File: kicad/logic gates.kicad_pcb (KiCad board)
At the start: 2 copper layers, 33 parts, among them J1 USB_B_Micro, Q1 NPN, Q2 NPN, Q3 NPN, Q4 NPN, Q5 NPN, Q6 NPN, Q7 NPN, SW1 SW_SPST, SW2 SW_SPST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

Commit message: pcb cleanup
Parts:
- moved J1 24.0 mm to (91.2, 16.4)
- moved SW6 23.0 mm to (82.0, 16.0)
- moved R11 2.01 mm to (134.5, 46.1), turned to 90 degrees
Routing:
- net Net-(D4-K): track 595.8 -> 547.7 mm
- net Net-(Q7-B): track 51.3 -> 64.4 mm
- net Net-(Q6-C): track 24.8 -> 26.4 mm
- net Net-(D3-K): track 291.1 -> 292.5 mm
- net Net-(J1-VBUS): track 9.02 -> 9.92 mm
- net Net-(D1-K): track 51.5 -> 50.8 mm

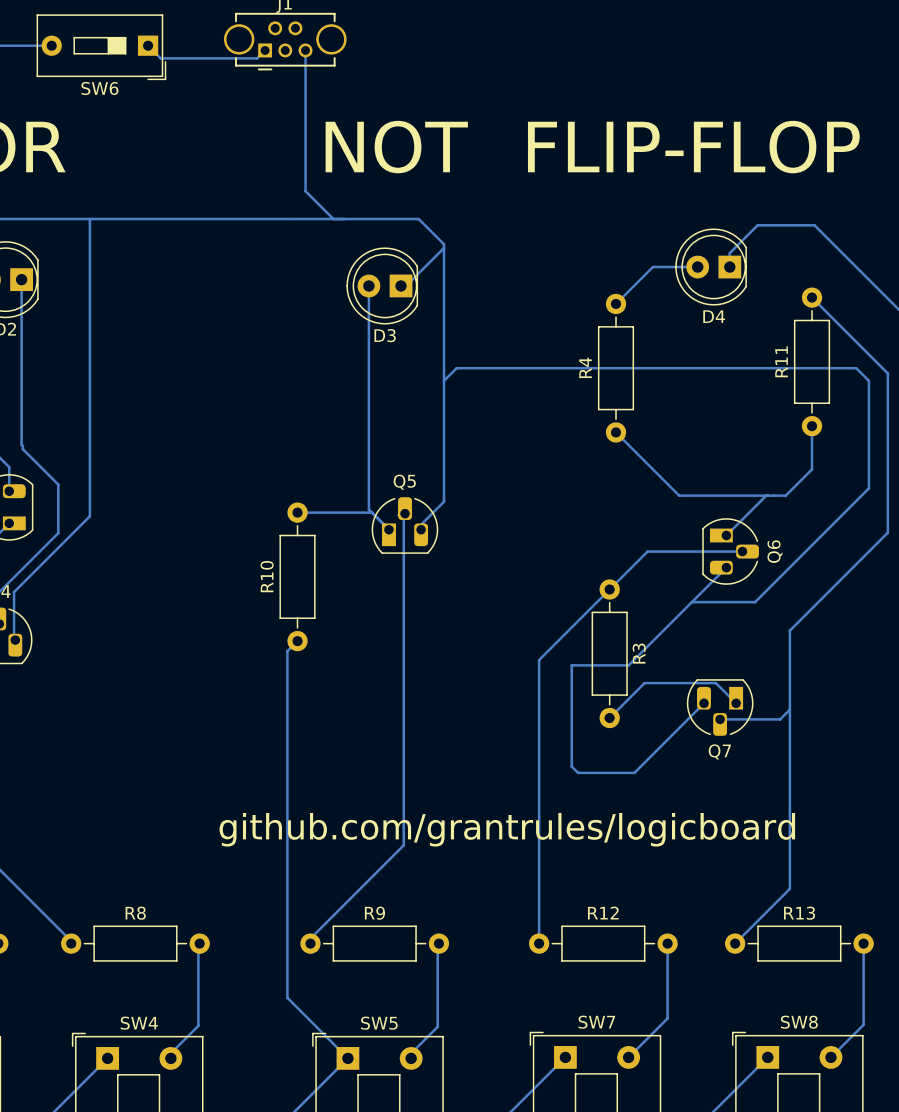
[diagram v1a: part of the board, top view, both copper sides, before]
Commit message: fixed names and values
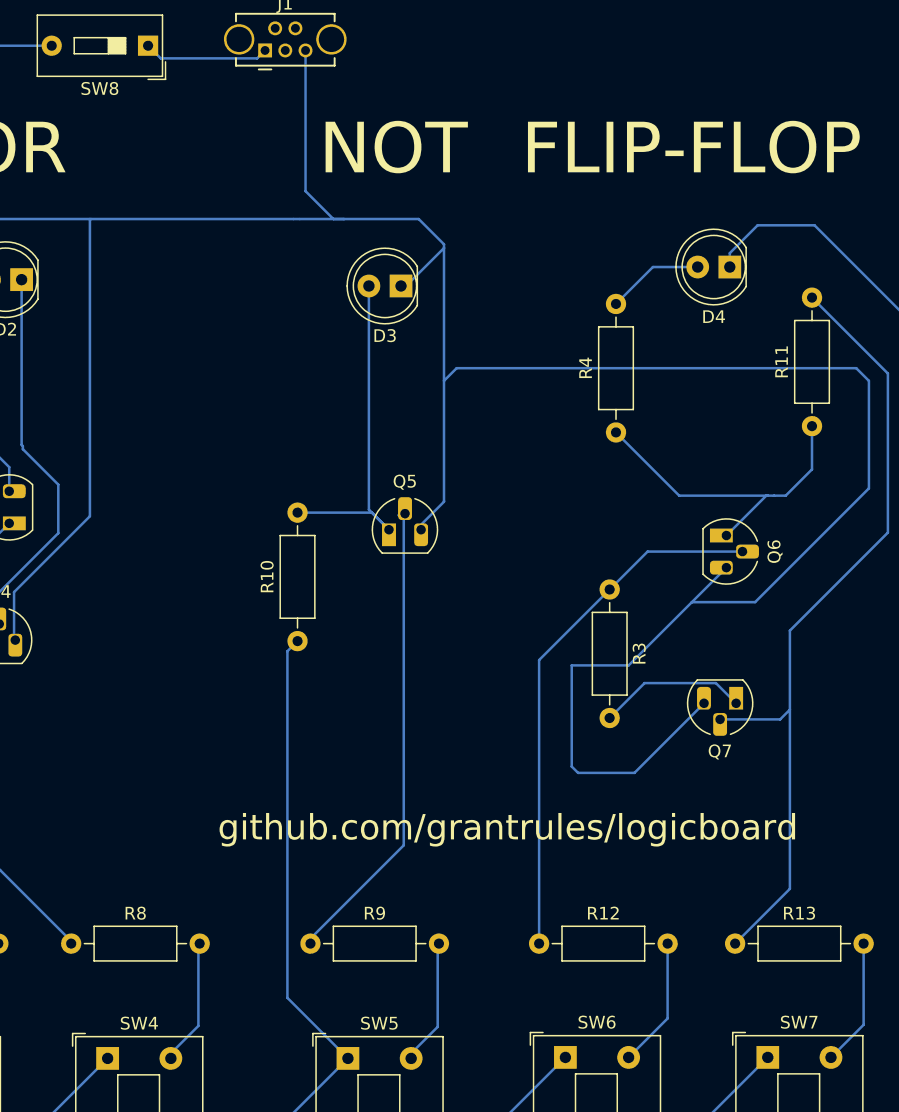
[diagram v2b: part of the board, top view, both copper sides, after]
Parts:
- R10: value 350 -> 345
- R2, R4: value R345 -> 345
- renumbered SW7 to SW6, SW8 to SW7, SW6 to SW8
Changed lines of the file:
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@@
 	(net 28 "Net-(Q7-C)")
 	(net 29 "Net-(SW7-B)")
-	(net 30 "Net-(SW8-B)")
+	(net 30 "Net-(SW6-B)")
 	(footprint "LED_THT:LED_D5.0mm"
 		(layer "F.Cu")
@@
 			)
 		)
-		(property "Value" "R345"
+		(property "Value" "345"
 			(at 5.08 2.37 90)
 			(layer "F.Fab")
@@
 			)
 		)
-		(property "Value" "350"
+		(property "Value" "345"
 			(at 5.08 2.37 90)
 			(layer "F.Fab")
@@
 			(layers "*.Cu" "*.Mask")
 			(remove_unused_layers no)
-			(net 29 "Net-(SW7-B)")
+			(net 30 "Net-(SW6-B)")
 			(pintype "passive")
 		)
@@
 		(descr "momentary / push-push button, h=17.5mm C&K PVA1 https://www.ckswitches.com/media/1343/pva.pdf")
 		(tags "tact sw push PVA1 DPST")
-		(property "Reference" "SW7"
+		(property "Reference" "SW6"
 			(at 2.5 -2.75 0)
 			(layer "F.SilkS")
@@
 			(layers "*.Cu" "*.Mask")
 			(remove_unused_layers no)
-			(net 29 "Net-(SW7-B)")
+			(net 30 "Net-(SW6-B)")
 			(pinfunction "B")
 			(pintype "passive")
@@
 			(layers "*.Cu" "*.Mask")
 			(remove_unused_layers no)
-			(net 30 "Net-(SW8-B)")
+			(net 29 "Net-(SW7-B)")
 			(pintype "passive")
 		)
@@
 		(descr "1x-dip-switch SPST , Slide, row spacing 7.62 mm (300 mils), body size 9.78x4.72mm (see e.g. https://www.ctscorp.com/wp-content/uploads/206-208.pdf)")
 		(tags "DIP Switch SPST Slide 7.62mm 300mil")
-		(property "Reference" "SW6"
+		(property "Reference" "SW8"
 			(at 3.81 -3.42 0)
 			(layer "F.SilkS")
@@
 		(descr "momentary / push-push button, h=17.5mm C&K PVA1 https://www.ckswitches.com/media/1343/pva.pdf")
 		(tags "tact sw push PVA1 DPST")
-		(property "Reference" "SW8"
+		(property "Reference" "SW7"
 			(at 2.5 -2.75 0)
 			(layer "F.SilkS")
@@
 			(layers "*.Cu" "*.Mask")
 			(remove_unused_layers no)
-			(net 30 "Net-(SW8-B)")
+			(net 29 "Net-(SW7-B)")
 			(pinfunction "B")
 			(pintype "passive")
@@
 			)
 		)
-		(property "Value" "R345"
+		(property "Value" "345"
 			(at 5.08 2.37 90)
 			(layer "F.Fab")
@@
 	)
 	(segment
-		(start 123.08 92.92)
-		(end 123.08 87)
+		(start 138.58 93.42)
+		(end 138.58 87)
 		(width 0.2)
 		(layer "B.Cu")
@@
 	)
 	(segment
-		(start 120 96)
-		(end 123.08 92.92)
+		(start 136 96)
+		(end 138.58 93.42)
 		(width 0.2)
 		(layer "B.Cu")
@@
 	)
 	(segment
-		(start 138.58 93.42)
-		(end 138.58 87)
+		(start 123.08 92.92)
+		(end 123.08 87)
 		(width 0.2)
 		(layer "B.Cu")
@@
 	)
 	(segment
-		(start 136 96)
-		(end 138.58 93.42)
+		(start 120 96)
+		(end 123.08 92.92)
 		(width 0.2)
 		(layer "B.Cu")

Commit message: fix pcb
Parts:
- J1: value USB_B_Micro -> USB_C_2PIN; footprint Connector_USB:USB_Mini-B_Tensility_54-00023_Vertical_CircularHoles -> Aliexpress crap:USB_C_2pin-aliexpress
- SW1, SW2, SW3, SW4, SW5, SW6, SW7: footprint Button_Switch_THT:SW_Push_2P1T_Toggle_CK_PVA1xxH1xxxxxxV2 -> Button_Switch_THT:SW_PUSH_6mm_H5mm
- SW8: footprint Button_Switch_THT:SW_DIP_SPSTx01_Slide_9.78x4.72mm_W7.62mm_P2.54mm -> Button_Switch_THT:SW_CK_JS202011CQN_DPDT_Straight
- moved SW8 3.61 mm to (79.0, 18.0)
- moved D4 1.00 mm to (128.0, 34.5)
- moved J1 0.80 mm to (91.3, 15.6), turned to 180 degrees
- moved D3 0.50 mm to (102.0, 34.5)
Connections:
- SW8 pad 1: Net-(J1-VBUS) -> Net-(J1-GND)
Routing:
- net Net-(J1-GND): track 0.00 -> 13.2 mm
- net Net-(J1-VBUS): track 9.92 -> 0.00 mm
- net Net-(SW4-B): track 10.0 -> 17.6 mm
- net Net-(SW5-B): track 9.99 -> 15.9 mm
- net Net-(SW3-B): track 10.1 -> 15.9 mm
- net Net-(SW1-B): track 10.1 -> 15.9 mm
- net Net-(SW6-B): track 10.3 -> 15.9 mm
- net Net-(SW2-B): track 10.1 -> 15.5 mm
- net Net-(SW7-B): track 10.1 -> 14.6 mm
- net Net-(D4-K): track 547.7 -> 550.9 mm
- net Net-(D3-K): track 292.5 -> 289.4 mm
- net (no net): track 0.88 -> 0.00 mm
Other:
- board outline added: 130 x 100 mm

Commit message: fixed usb port, added versioning
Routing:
- net Net-(D2-K): track 42.0 -> 36.6 mm
- net Net-(J1-GND): track 13.2 -> 15.1 mm
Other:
- board text added: "logicbuddy v0.1 github.com/grantrules/logicbuddy"
- board text removed: "github.com/grantrules/logicboard"
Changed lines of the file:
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@@
 		(tags "tact sw push 6mm")
 		(property "Reference" "SW1"
-			(at 3.25 -2 360)
+			(at 3.25 -2 0)
 			(layer "F.SilkS")
 			(effects
@@
 		)
 		(property "Value" "SW_SPST"
-			(at 3.75 6.7 360)
+			(at 3.75 6.7 0)
 			(layer "F.Fab")
 			(effects
@@
 		)
 		(fp_text user "${REFERENCE}"
-			(at 3.25 2.25 360)
+			(at 3.25 2.25 0)
 			(layer "F.Fab")
 			(effects
@@
 		)
 		(pad "A1" thru_hole roundrect
-			(at -2 -3.6 180)
+			(at 2 -3.3 180)
 			(size 2.1 1.1)
-			(drill oval 1.7 0.7)
+			(drill oval 1.5 0.7)
 			(layers "*.Cu" "*.Mask")
 			(remove_unused_layers no)
@@
 		)
 		(pad "A4" thru_hole roundrect
-			(at 2 -3.6 180)
+			(at -2 -3.3 180)
 			(size 2.1 1.1)
-			(drill oval 1.7 0.7)
+			(drill oval 1.5 0.7)
 			(layers "*.Cu" "*.Mask")
 			(remove_unused_layers no)
@@
 		(layer "Edge.Cuts")
 	)
-	(gr_text "github.com/grantrules/logicboard"
+	(gr_text "logicbuddy v0.1\ngithub.com/grantrules/logicbuddy"
 		(at 87.5 79 0)
 		(layer "F.SilkS")
@@
 	)
 	(segment
+		(start 68.86 60.584208)
+		(end 70.972104 58.472104)
+		(width 0.2)
+		(layer "B.Cu")
+		(net 3)
+	)
+	(segment
+		(start 71.02 58.424208)
+		(end 70.972104 58.472104)
+		(width 0.2)
+		(layer "B.Cu")
+		(net 3)
+	)
+	(segment
 		(start 74.9 50.46)
 		(end 72 47.56)
@@
 	)
 	(segment
-		(start 68.86 60.584208)
-		(end 74.9 54.544208)
-		(width 0.2)
-		(layer "B.Cu")
-		(net 3)
-	)
-	(segment
-		(start 71.02 53.77)
-		(end 68.96 55.83)
-		(width 0.2)
-		(layer "B.Cu")
-		(net 3)
-	)
-	(segment
 		(start 74.9 54.544208)
 		(end 74.9 50.46)
@@
 	)
 	(segment
-		(start 68.96 55.83)
-		(end 68.96 63)
+		(start 71.02 53.77)
+		(end 71.02 58.424208)
 		(width 0.2)
 		(layer "B.Cu")
@@
 	)
 	(segment
+		(start 70.972104 58.472104)
+		(end 74.9 54.544208)
+		(width 0.2)
+		(layer "B.Cu")
+		(net 3)
+	)
+	(segment
 		(start 68.86 62.705)
 		(end 68.86 60.584208)
@@
 	)
 	(segment
+		(start 89.32 29.525)
+		(end 89.5 29.705)
+		(width 0.2)
+		(layer "B.Cu")
+		(net 6)
+	)
+	(segment
 		(start 71.4 62.705)
 		(end 71.4 59.205)
@@
 	)
 	(segment
+		(start 89.32 18.775)
+		(end 89.32 29.525)
+		(width 0.2)
+		(layer "B.Cu")
+		(net 6)
+	)
+	(segment
 		(start 106.4 41.5)
 		(end 105.4 42.5)
@@
 	)
 	(segment
-		(start 92 20.495)
-		(end 92 29.705)
-		(width 0.2)
-		(layer "B.Cu")
-		(net 6)
-	)
-	(segment
-		(start 93.32 19.175)
-		(end 92 20.495)
-		(width 0.2)
-		(layer "B.Cu")
-		(net 6)
-	)
-	(segment
 		(start 139 51)
 		(end 139 42.5)
@@
 	)
 	(segment
-		(start 87.495 21)
-		(end 89.32 19.175)
+		(start 92.045 17.5)
+		(end 93.32 18.775)
 		(width 0.2)
 		(layer "B.Cu")
@@
 	)
 	(segment
-		(start 80.5 21)
-		(end 87.495 21)
+		(start 79 18)
+		(end 79.5 17.5)
 		(width 0.2)
 		(layer "B.Cu")
@@
 	)
 	(segment
-		(start 79 18)
-		(end 79 19.5)
-		(width 0.2)
-		(layer "B.Cu")
-		(net 20)
-	)
-	(segment
-		(start 79 19.5)
-		(end 80.5 21)
-		(width 0.2)
-		(layer "B.Cu")
+		(start 79.5 17.5)
+		(end 92.045 17.5)
+		(width 0.2)
+		(layer "B.Cu")
